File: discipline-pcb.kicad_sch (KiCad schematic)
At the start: 203 parts, among them SW1 KEYSW, SW10 KEYSW, SW11 KEYSW, SW12 KEYSW, SW13 KEYSW, SW14 KEYSW, SW16 KEYSW, SW17 KEYSW, SW18 KEYSW, SW19 KEYSW, SW2 KEYSW, SW20 KEYSW, SW21 KEYSW, SW22 KEYSW, SW23 KEYSW, SW24 KEYSW, SW25 KEYSW, SW26 KEYSW, SW27 KEYSW, SW28 KEYSW, SW29 KEYSW, SW3 KEYSW, SW31 KEYSW, SW32 KEYSW, SW33 KEYSW, SW34 KEYSW, SW35 KEYSW, SW36 KEYSW, SW37 KEYSW, SW38 KEYSW, SW39 KEYSW, SW4 KEYSW, SW40 KEYSW, SW41 KEYSW, SW42 KEYSW, SW43 KEYSW, SW45 KEYSW, SW46 KEYSW, SW47 KEYSW, SW48 KEYSW, SW49 KEYSW, SW5 KEYSW, SW50 KEYSW, SW51 KEYSW, SW52 KEYSW, SW53 KEYSW, SW54 KEYSW, SW55 KEYSW, SW56 KEYSW, SW57 KEYSW, SW59 KEYSW, SW6 KEYSW, SW60 KEYSW, SW61 KEYSW, SW62 KEYSW, SW7 KEYSW, SW72 KEYSW, SW73 KEYSW, SW74 KEYSW, SW75 KEYSW, SW76 KEYSW, SW77 KEYSW, SW78 KEYSW, SW79 KEYSW, SW8 KEYSW, SW80 KEYSW, SW81 KEYSW, SW82 KEYSW, SW83 KEYSW, SW9 KEYSW, U1 SN74AHCT125N

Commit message: more routing
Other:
- moved on the sheet: A1, C1, C10, C11, C12, C13, C14, C15, C16, C17, C18, C19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

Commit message: after advice on usb implementation
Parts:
- removed A1: RaspberryPi_Pico, cftkb:RaspberryPi_CPico, symbol MCU_Module:RaspberryPi_Pico
- added D69, D70: 3.6V, cftkb:D_DO-35_SOD27_P5.08mm_Horizontal, symbol Device:D_Zener_Small
- added F1: 500mA, cftkb:polyfuse_5.1mm, symbol Device:Polyfuse_Small
- added R1, R2: 5.1k, cftkb:R_Axial_DIN0204_L3.6mm_D1.6mm_P7.62mm_Horizontal, symbol Device:R_Small
- added SW-RST2: ~, cftkb:SW_PUSH_6mm, symbol Switch:SW_Push
- added U2: RP2040_Stamp, RP2xxx_Stamp:RP2xxx_Stamp_SMD, symbol RP2xxx_Stamp:RP2040_Stamp
- added USB1: USB_C_GCT_USB4085, cftkb:USB_C_GCT_USB4085, symbol discipline-pcb-rescue:USB_C_GCT_USB4085-Type-C
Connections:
- net +5V: now also LED1.1 (VDD), LED10.1 (VDD), LED11.1 (VDD), LED12.1 (VDD), LED13.1 (VDD), LED14.1 (VDD), LED15.1 (VDD), LED16.1 (VDD), LED17.1 (VDD), LED18.1 (VDD), LED19.1 (VDD), LED2.1 (VDD), LED20.1 (VDD), LED21.1 (VDD), LED22.1 (VDD), LED23.1 (VDD), LED24.1 (VDD), LED25.1 (VDD), LED26.1 (VDD), LED27.1 (VDD), LED28.1 (VDD), LED29.1 (VDD), LED3.1 (VDD), LED30.1 (VDD), LED4.1 (VDD), LED5.1 (VDD), LED6.1 (VDD), LED7.1 (VDD), LED8.1 (VDD), LED9.1 (VDD), F1.1, U2.33 (5V)
- net GND: now also D69.2 (A), D70.2 (A), R1.1, R2.2, SW-RST2.2, U2.31 (GND), USB1.A1 (GND), USB1.A12 (GND), USB1.B1 (GND), USB1.B12 (GND), USB1.S1 (SHIELD)
- net Resetbtn: now also U2.39 (~{RESET})
- net VSYS: no longer LED1.1 (VDD), LED10.1 (VDD), LED11.1 (VDD), LED12.1 (VDD), LED13.1 (VDD), LED14.1 (VDD), LED15.1 (VDD), LED16.1 (VDD), LED17.1 (VDD), LED18.1 (VDD), LED19.1 (VDD), LED2.1 (VDD), LED20.1 (VDD), LED21.1 (VDD), LED22.1 (VDD), LED23.1 (VDD), LED24.1 (VDD), LED25.1 (VDD), LED26.1 (VDD), LED27.1 (VDD), LED28.1 (VDD), LED29.1 (VDD), LED3.1 (VDD), LED30.1 (VDD), LED4.1 (VDD), LED5.1 (VDD), LED6.1 (VDD), LED7.1 (VDD), LED8.1 (VDD), LED9.1 (VDD)
- net col0: now also U2.16 (GPIO15)
- net col1: now also U2.15 (GPIO14)
- net col10: now also U2.6 (GPIO5)
- net col11: now also U2.5 (GPIO4)
- net col12: now also U2.4 (GPIO3)
- net col13: now also U2.17 (GPIO16)
- net col14: now also U2.3 (GPIO2)
- net col15: now also U2.2 (GPIO1)
- net col16: now also U2.1 (GPIO0)
- net col2: now also U2.14 (GPIO13)
- net col3: now also U2.13 (GPIO12)
- net col4: now also U2.12 (GPIO11)
- net col5: now also U2.11 (GPIO10)
- net col6: now also U2.10 (GPIO9)
- net col7: now also U2.9 (GPIO8)
- net col8: now also U2.8 (GPIO7)
- net col9: now also U2.7 (GPIO6)
- net ledpin: now also U2.18 (GPIO17)
- net row0: now also U2.22 (GPIO21)
- net row1: now also U2.21 (GPIO20)
- net row2: now also U2.19 (GPIO18)
- net row3: now also U2.23 (GPIO22)
- net row4: now also U2.20 (GPIO19)
- new net: R1.2, USB1.A5 (CC1)
- new net: R2.1, USB1.B5 (CC2)
- new net Bootselbtn: SW-RST2.1, U2.40 (BOOTSEL)
- new net D+: D70.1 (K), U2.36 (USB_D+), USB1.A6 (DP1), USB1.B6 (DP2)
- new net D-: D69.1 (K), U2.35 (USB_D-), USB1.A7 (DN1), USB1.B7 (DN2)
- new net VCC: F1.2, USB1.A4 (VBUS), USB1.A9 (VBUS), USB1.B4 (VBUS), USB1.B9 (VBUS)
- no-connect marks 1 -> 2
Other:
- moved on the sheet: C1, C10, C11, C12, C13, C14, C15, C16, C17, C18, C19, C2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

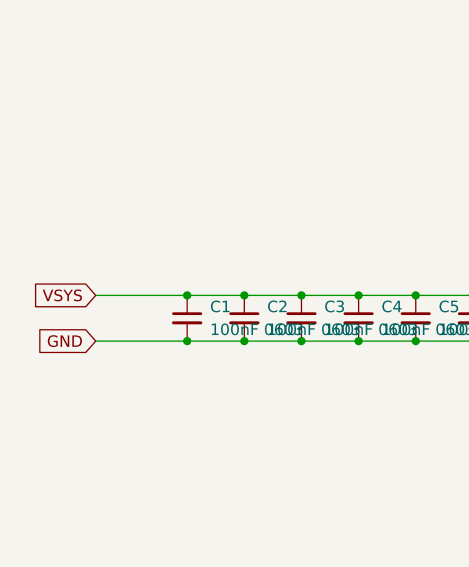
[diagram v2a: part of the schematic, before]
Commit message: continue routing and adding LEDs
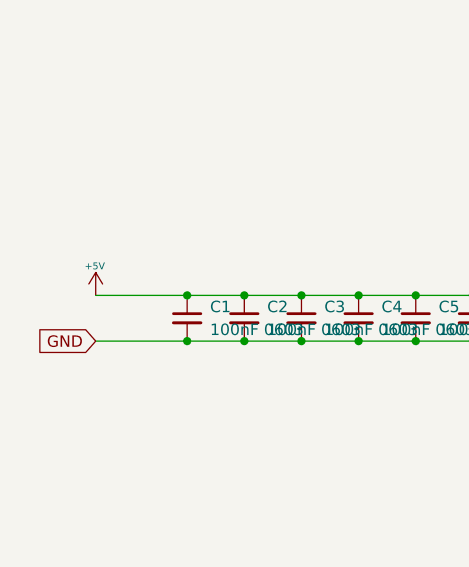
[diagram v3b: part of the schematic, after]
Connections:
- net VSYS is gone; now on net +5V: C1.1, C10.1, C11.1, C12.1, C13.1, C14.1, C15.1, C16.1, C17.1, C18.1, C19.1, C2.1, C20.1, C21.1, C22.1, C23.1, C24.1, C25.1, C26.1, C27.1, C28.1, C29.1, C3.1, C30.1, C4.1, C5.1, C6.1, C7.1, C8.1, C9.1
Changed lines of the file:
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@@
 		)
 	)
-	(global_label "VSYS"
-		(shape input)
-		(at 22.86 233.68 180)
-		(fields_autoplaced yes)
-		(effects
-			(font
-				(size 1.27 1.27)
-			)
-			(justify right)
-		)
-		(property "Intersheetrefs" "${INTERSHEET_REFS}"
-			(at 15.9328 233.68 0)
-			(effects
-				(font
-					(size 1.27 1.27)
-				)
-				(justify right)
-				(hide yes)
-			)
-		)
-	)
 	(global_label "col13"
 		(shape input)
@@
 					(unit 1)
 				)
+			)
+		)
+	)
+	(symbol
+		(lib_id "discipline-pcb-rescue:+5V-power")
+		(at 22.86 233.68 0)
+		(unit 1)
+		(exclude_from_sim no)
+		(in_bom yes)
+		(on_board yes)
+		(dnp no)
+		(property "Reference" "#PWR0127"
+			(at 22.86 231.394 0)
+			(effects
+				(font
+					(size 0.508 0.508)
+				)
+				(hide yes)
+			)
+		)
+		(property "Value" "+5V"
+			(at 22.7584 230.4288 0)
+			(effects
+				(font
+					(size 0.762 0.762)
+				)
+			)
+		)
+		(property "Footprint" ""
+			(at 22.86 233.68 0)
+			(effects
+				(font
+					(size 1.524 1.524)
+				)
+			)
+		)
+		(property "Datasheet" ""
+			(at 22.86 233.68 0)
+			(effects
+				(font
+					(size 1.524 1.524)
+				)
+			)
+		)
+		(property "Description" ""
+			(at 22.86 233.68 0)
+			(effects
+				(font
+					(size 1.27 1.27)
+				)
+			)
+		)
+		(pin "1"
+		)
+		(instances
+			(project "discipline-pcb"
+				(path "/92ddd8bc-b115-4355-8708-2687f9ad53cd"
+					(reference "#PWR0127")
+					(unit 1)
+				)

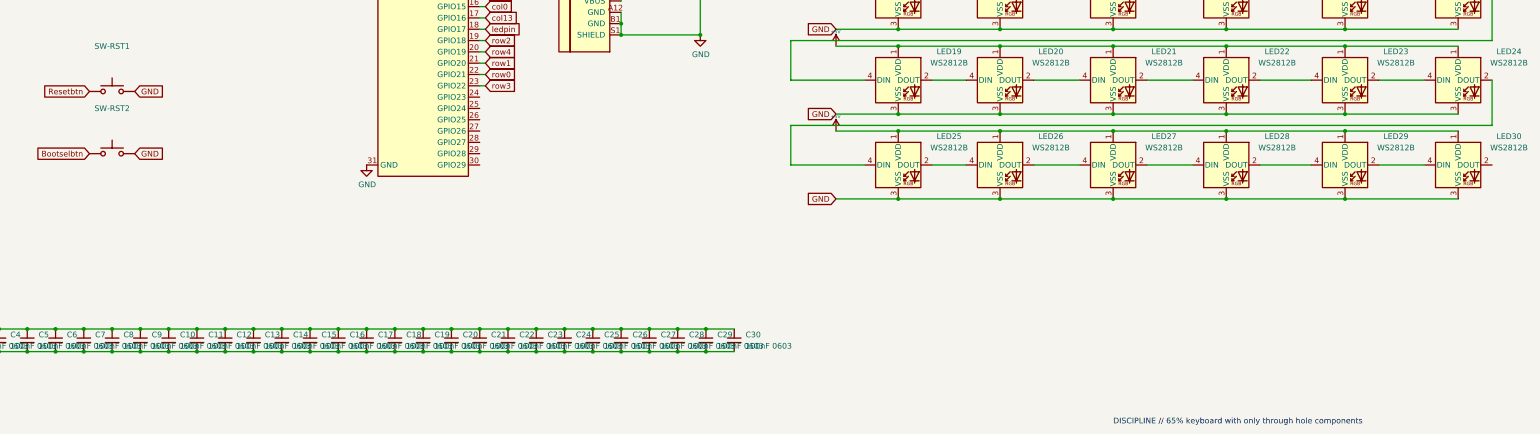
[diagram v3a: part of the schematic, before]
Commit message: leds placed, diodes and MCU left...
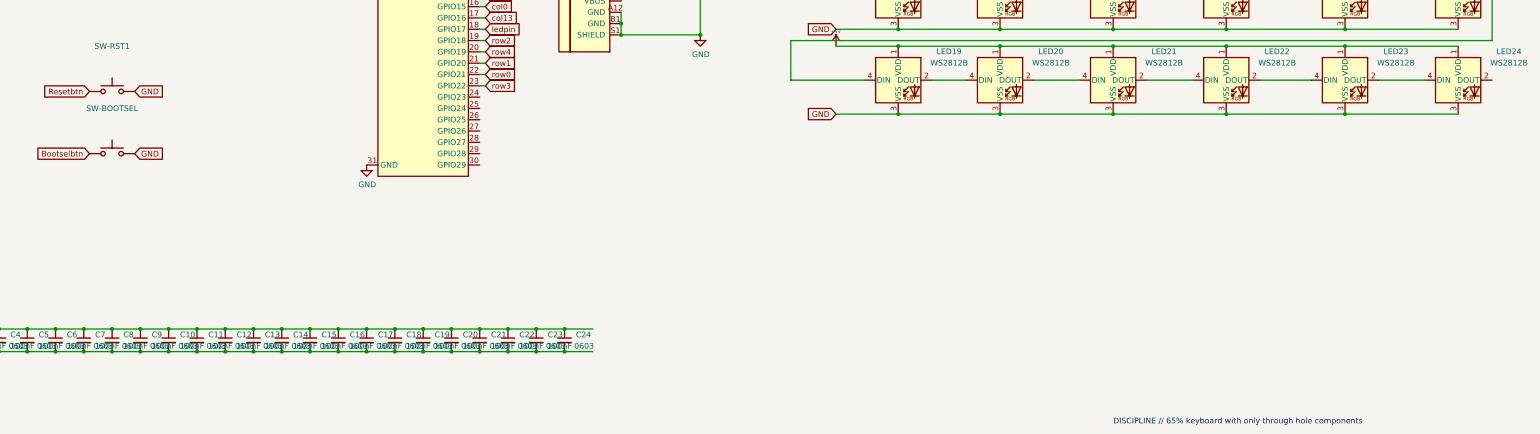
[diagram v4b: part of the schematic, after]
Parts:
- removed C25, C26, C27, C28, C29, C30: 100nF 0603, Capacitor_SMD:C_0603_1608Metric_Pad1.08x0.95mm_HandSolder, symbol Device:C_Small
- removed LED25, LED26, LED27, LED28, LED29, LED30: WS2812B, LED_SMD:LED_WS2812B_PLCC4_5.0x5.0mm_P3.2mm, symbol LED:WS2812B
- renumbered SW-RST2 to SW-BOOTSEL

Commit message: more routing
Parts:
- renumbered SW-BOOTSEL to SW-BOOTSEL1
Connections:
- net col0: now also U2.25 (GPIO24); no longer U2.16 (GPIO15)
- net col1: now also U2.24 (GPIO23); no longer U2.15 (GPIO14)
- net col10: now also U2.15 (GPIO14); no longer U2.6 (GPIO5)
- net col11: now also U2.13 (GPIO12); no longer U2.5 (GPIO4)
- net col12: now also U2.14 (GPIO13); no longer U2.4 (GPIO3)
- net col13: now also U2.12 (GPIO11); no longer U2.17 (GPIO16)
- net col16: now also U2.4 (GPIO3); no longer U2.1 (GPIO0)
- net col2: now also U2.23 (GPIO22); no longer U2.14 (GPIO13)
- net col3: now also U2.22 (GPIO21); no longer U2.13 (GPIO12)
- net col4: now also U2.21 (GPIO20); no longer U2.12 (GPIO11)
- net col5: now also U2.20 (GPIO19); no longer U2.11 (GPIO10)
- net col6: now also U2.19 (GPIO18); no longer U2.10 (GPIO9)
- net col7: now also U2.18 (GPIO17); no longer U2.9 (GPIO8)
- net col8: now also U2.17 (GPIO16); no longer U2.8 (GPIO7)
- net col9: now also U2.16 (GPIO15); no longer U2.7 (GPIO6)
- net ledpin: now also U2.1 (GPIO0); no longer U2.18 (GPIO17)
- net row0: now also U2.30 (GPIO29); no longer U2.22 (GPIO21)
- net row1: now also U2.29 (GPIO28); no longer U2.21 (GPIO20)
- net row2: now also U2.26 (GPIO25); no longer U2.19 (GPIO18)
- net row3: now also U2.28 (GPIO27); no longer U2.23 (GPIO22)
- net row4: now also U2.27 (GPIO26); no longer U2.20 (GPIO19)
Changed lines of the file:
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@@
 	(global_label "row4"
 		(shape input)
-		(at 161.29 171.45 0)
+		(at 160.02 189.23 0)
 		(fields_autoplaced yes)
 		(effects
@@
 		)
 		(property "Intersheetrefs" "${INTERSHEET_REFS}"
-			(at 168.0962 171.45 0)
+			(at 166.8262 189.23 0)
 			(effects
 				(font
@@
 	(global_label "col6"
 		(shape input)
-		(at 161.29 146.05 0)
+		(at 161.29 168.91 0)
 		(fields_autoplaced yes)
 		(effects
@@
 		)
 		(property "Intersheetrefs" "${INTERSHEET_REFS}"
-			(at 167.7333 146.05 0)
+			(at 167.7333 168.91 0)
 			(effects
 				(font
@@
 	(global_label "col0"
 		(shape input)
-		(at 161.29 161.29 0)
+		(at 160.02 184.15 0)
 		(fields_autoplaced yes)
 		(effects
@@
 		)
 		(property "Intersheetrefs" "${INTERSHEET_REFS}"
-			(at 167.7333 161.29 0)
+			(at 167.6728 184.15 0)
 			(effects
 				(font
@@
 	(global_label "col2"
 		(shape input)
-		(at 161.29 156.21 0)
+		(at 161.29 179.07 0)
 		(fields_autoplaced yes)
 		(effects
@@
 		)
 		(property "Intersheetrefs" "${INTERSHEET_REFS}"
-			(at 167.7333 156.21 0)
+			(at 167.7333 179.07 0)
 			(effects
 				(font
@@
 	(global_label "col11"
 		(shape input)
-		(at 161.29 133.35 0)
+		(at 161.29 153.67 0)
 		(fields_autoplaced yes)
 		(effects
@@
 		)
 		(property "Intersheetrefs" "${INTERSHEET_REFS}"
-			(at 168.9428 133.35 0)
+			(at 168.9428 153.67 0)
 			(effects
 				(font
@@
 	(global_label "col7"
 		(shape input)
-		(at 161.29 143.51 0)
+		(at 161.29 166.37 0)
 		(fields_autoplaced yes)
 		(effects
@@
 		)
 		(property "Intersheetrefs" "${INTERSHEET_REFS}"
-			(at 167.7333 143.51 0)
+			(at 167.7333 166.37 0)
 			(effects
 				(font
@@
 	(global_label "row2"
 		(shape input)
-		(at 161.29 168.91 0)
+		(at 160.02 186.69 0)
 		(fields_autoplaced yes)
 		(effects
@@
 		)
 		(property "Intersheetrefs" "${INTERSHEET_REFS}"
-			(at 168.0962 168.91 0)
+			(at 166.8262 186.69 0)
 			(effects
 				(font
@@
 	(global_label "row3"
 		(shape input)
-		(at 161.29 179.07 0)
+		(at 160.02 191.77 0)
 		(fields_autoplaced yes)
 		(effects
@@
 		)
 		(property "Intersheetrefs" "${INTERSHEET_REFS}"
-			(at 168.0962 179.07 0)
+			(at 166.8262 191.77 0)
 			(effects
 				(font
@@
 	(global_label "row0"
 		(shape input)
-		(at 161.29 176.53 0)
+		(at 160.02 196.85 0)
 		(fields_autoplaced yes)
 		(effects
@@
 		)
 		(property "Intersheetrefs" "${INTERSHEET_REFS}"
-			(at 168.0962 176.53 0)
+			(at 166.8262 196.85 0)
 			(effects
 				(font
@@
 	(global_label "col8"
 		(shape input)
-		(at 161.29 140.97 0)
+		(at 161.29 163.83 0)
 		(fields_autoplaced yes)
 		(effects
@@
 		)
 		(property "Intersheetrefs" "${INTERSHEET_REFS}"
-			(at 167.7333 140.97 0)
+			(at 167.7333 163.83 0)
 			(effects
 				(font
@@
 	(global_label "col9"
 		(shape input)
-		(at 161.29 138.43 0)
+		(at 161.29 161.29 0)
 		(fields_autoplaced yes)
 		(effects
@@
 		)
 		(property "Intersheetrefs" "${INTERSHEET_REFS}"
-			(at 167.7333 138.43 0)
+			(at 167.7333 161.29 0)
 			(effects
 				(font
@@
 	(global_label "col10"
 		(shape input)
-		(at 161.29 135.89 0)
+		(at 161.29 158.75 0)
 		(fields_autoplaced yes)
 		(effects
@@
 		)
 		(property "Intersheetrefs" "${INTERSHEET_REFS}"
-			(at 168.9428 135.89 0)
+			(at 168.9428 158.75 0)
 			(effects
 				(font
@@
 	(global_label "col5"
 		(shape input)
-		(at 161.29 148.59 0)
+		(at 161.29 171.45 0)
 		(fields_autoplaced yes)
 		(effects
@@
 		)
 		(property "Intersheetrefs" "${INTERSHEET_REFS}"
-			(at 167.7333 148.59 0)
+			(at 167.7333 171.45 0)
 			(effects
 				(font
@@
 	(global_label "col16"
 		(shape input)
-		(at 161.29 123.19 0)
+		(at 161.29 130.81 0)
 		(fields_autoplaced yes)
 		(effects
@@
 		)
 		(property "Intersheetrefs" "${INTERSHEET_REFS}"
-			(at 168.9428 123.19 0)
+			(at 168.9428 130.81 0)
 			(effects
 				(font
@@
 	(global_label "col3"
 		(shape input)
-		(at 161.29 153.67 0)
+		(at 161.29 176.53 0)
 		(fields_autoplaced yes)
 		(effects
@@
 		)
 		(property "Intersheetrefs" "${INTERSHEET_REFS}"
-			(at 167.7333 153.67 0)
+			(at 167.7333 176.53 0)
 			(effects
 				(font
@@
 	(global_label "col1"
 		(shape input)
-		(at 161.29 158.75 0)
+		(at 160.02 181.61 0)
 		(fields_autoplaced yes)
 		(effects
@@
 		)
 		(property "Intersheetrefs" "${INTERSHEET_REFS}"
-			(at 167.7333 158.75 0)
+			(at 166.4633 181.61 0)
 			(effects
 				(font
@@
 	(global_label "ledpin"
 		(shape input)
-		(at 161.29 166.37 0)
+		(at 161.29 123.19 0)
 		(fields_autoplaced yes)
 		(effects
@@
 		)
 		(property "Intersheetrefs" "${INTERSHEET_REFS}"
-			(at 169.4266 166.37 0)
+			(at 169.4266 123.19 0)
 			(effects
 				(font
@@
 	(global_label "col12"
 		(shape input)
-		(at 161.29 130.81 0)
+		(at 161.29 156.21 0)
 		(fields_autoplaced yes)
 		(effects
@@
 		)
 		(property "Intersheetrefs" "${INTERSHEET_REFS}"
-			(at 168.9428 130.81 0)
+			(at 168.9428 156.21 0)
 			(effects
 				(font
@@
 	(global_label "row1"
 		(shape input)
-		(at 161.29 173.99 0)
+		(at 160.02 194.31 0)
 		(fields_autoplaced yes)
 		(effects
@@
 		)
 		(property "Intersheetrefs" "${INTERSHEET_REFS}"
-			(at 168.0962 173.99 0)
+			(at 166.8262 194.31 0)
 			(effects
 				(font
@@
 	(global_label "col13"
 		(shape input)
-		(at 161.29 163.83 0)
+		(at 161.29 151.13 0)
 		(fields_autoplaced yes)
 		(effects
@@
 		)
 		(property "Intersheetrefs" "${INTERSHEET_REFS}"
-			(at 168.9428 163.83 0)
+			(at 167.7333 151.13 0)
 			(effects
 				(font
@@
 	(global_label "col4"
 		(shape input)
-		(at 161.29 151.13 0)
+		(at 161.29 173.99 0)
 		(fields_autoplaced yes)
 		(effects
@@
 		)
 		(property "Intersheetrefs" "${INTERSHEET_REFS}"
-			(at 167.7333 151.13 0)
+			(at 167.7333 173.99 0)
 			(effects
 				(font
@@
 		(on_board yes)
 		(dnp no)
-		(property "Reference" "SW-BOOTSEL"
+		(property "Reference" "SW-BOOTSEL1"
 			(at 77.47 184.15 0)
 			(effects
@@
 			(project "discipline-pcb"
 				(path "/92ddd8bc-b115-4355-8708-2687f9ad53cd"
-					(reference "SW-BOOTSEL")
+					(reference "SW-BOOTSEL1")
 					(unit 1)
 				)
